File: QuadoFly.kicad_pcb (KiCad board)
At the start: 2 copper layers, 40 x 45 mm, 68 parts, among them J1 USB_C_Receptacle, J10 Conn_01x04_Male, J13 Conn_01x30_Male, J2 Conn_01x02_Male, J3 Conn_01x02_Male, J4 Conn_01x02_Male, J5 Conn_01x02_Male, J6 Conn_01x02_Male, J7 Conn_01x02_Male, J8 Conn_01x04_Male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

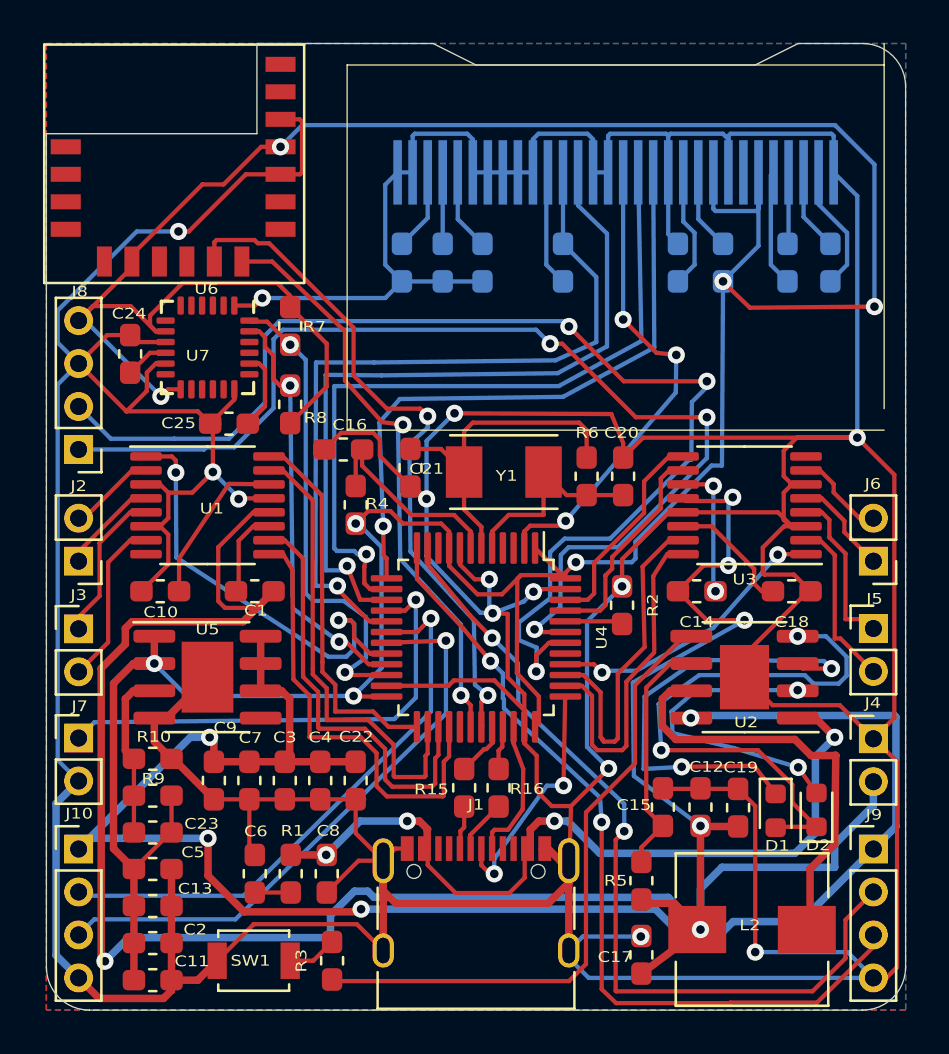
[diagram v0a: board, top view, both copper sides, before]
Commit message: 更新gerber文件，pcb 3d外观
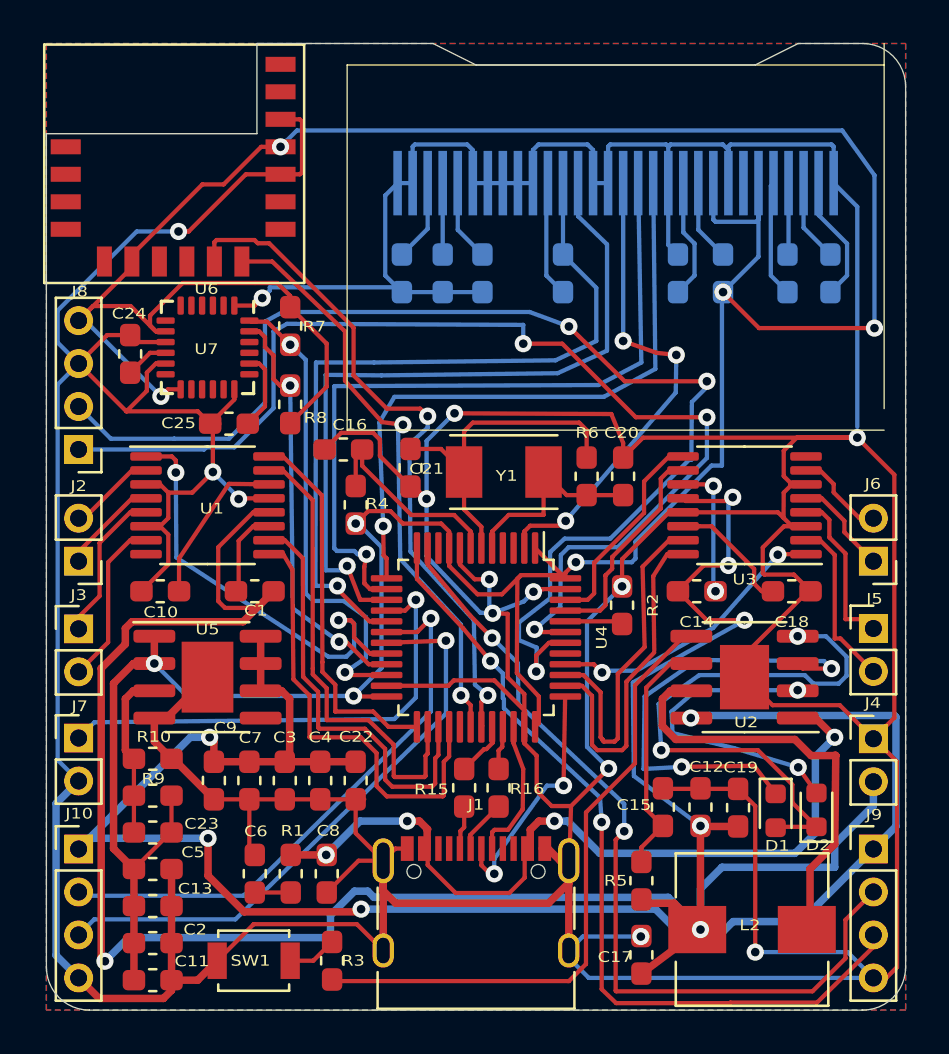
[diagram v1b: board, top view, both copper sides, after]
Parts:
- moved C26 0.50 mm to (136.5, 110.7)
- moved C27 0.50 mm to (134.5, 110.7)
- moved C28 0.50 mm to (116.5, 110.7)
- moved C29 0.50 mm to (118.5, 110.7)
- moved J13 0.50 mm to (126.5, 106.5)
- moved R11 0.50 mm to (124.0, 110.7)
- moved R12 0.50 mm to (120.3, 110.7)
- moved R13 0.50 mm to (131.5, 110.7)
- moved R14 0.50 mm to (129.4, 110.7)
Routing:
- net Earth: track 407.0 -> 405.5 mm
- net /+3.3V: track 177.9 -> 178.8 mm
- net /VL53_SDA: track 51.2 -> 52.1 mm
- net /OLED_MOSI: track 36.3 -> 35.7 mm
